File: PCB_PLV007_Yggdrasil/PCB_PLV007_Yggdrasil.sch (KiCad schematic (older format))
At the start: 16 parts

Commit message: Work on Heimdal and Yggdrasil
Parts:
- added C9, C? (x3): 0.1uF, symbol Device:C
- added C?: 1uF, symbol Device:C
- added D4, D?: LED, symbol Device:LED
- added JP?: Jumper_3_Open, symbol Jumper:Jumper_3_Open
- added Q4: Q_NMOS_GDS, symbol Device:Q_NMOS_GDS
- added Q5: Q_PMOS_GDS, symbol Device:Q_PMOS_GDS
- added R13, R18: 47K, symbol Device:R_US
- added R20, R? (x3): 1K, symbol Device:R_US
- added R22, R24, R28: 100K, symbol Device:R_US
- added R27: 700K, symbol Device:R_US
- added R? (x2): 10K, symbol Device:R_US
- added U7: BME280, Package_LGA:Bosch_LGA-8_2.5x2.5mm_P0.65mm_ClockwisePinNumbering, symbol Sensor:BME280
- added U?: 74HC21, Package_SO:SOIC-14_3.9x8.7mm_P1.27mm, symbol boringlib:74HC21
- added U? (x3): LM2902, symbol Amplifier_Operational:LM2902
- F1: renamed from F?; value Fuse -> 2A
- F2: renamed from F?; value Fuse -> 15A
- R21: renamed from R?; value R_US -> 1K
- R26: renamed from R?; value R_US -> 120
- gave numbers to parts that had none: 12
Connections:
- net labels added: +28V, C_SENSE, I2C_SCL, I2C_SDA, LOAD_SWITCH_ON, MCU_QB_INPUT, MCU_UHB_INPUT, UHB_MASTER, V_SENSE
- net labels removed: +24V, CURRENT_SENSE, LOAD_SWITCH_nON
- wire segments 75 -> 166
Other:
- moved on the sheet: C8, D1, F1, F2, J1, J2, JP1, NCLO1, Q3, R19, R21, R23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

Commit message: First version of Yggdrasil schematics complete
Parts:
- removed C9, C? (x2): 0.1uF, symbol Device:C
- removed D4, D?: LED, symbol Device:LED
- removed F2: 15A, symbol Device:Fuse
- removed J2: UMBILICAL_MASTER, symbol Connector_Generic:Conn_01x02
- removed Q3: Q_NPN_BCE, symbol Device:Q_NPN_BCE
- removed Q4: Q_NMOS_GDS, symbol Device:Q_NMOS_GDS
- removed Q5: Q_PMOS_GDS, symbol Device:Q_PMOS_GDS
- removed R20, R21, R? (x3): 1K, symbol Device:R_US
- removed R22, R24, R28: 100K, symbol Device:R_US
- removed R23: 2.7K, symbol Device:R_US
- removed R25, R? (x2): 10K, symbol Device:R_US
- removed R27: 700K, symbol Device:R_US
- removed U9: BTS50055-1TMA, Package_TO_SOT_SMD:TO-263-7_TabPin4, symbol Power_Management:BTS50055-1TMA
- removed U?: 74HC21, Package_SO:SOIC-14_3.9x8.7mm_P1.27mm, symbol boringlib:74HC21
- removed U? (x3): LM2902, symbol Amplifier_Operational:LM2902
- added C?: 0.1uF, symbol Device:C
- added C?: 10uF, symbol Device:C
- added C?: 1uF, symbol Device:C
- added R? (x3): 0, symbol Device:R_US
- added VR?: R-78C12-1.0, BoringFootprints:Recom_R-78c-1.0, symbol boringlib:R-78C12-1.0
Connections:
- net UMBILICAL_HEARTBEAT is gone; now on net UHB: R19.2
- net +12V: now also C?.1, C?.1, VR?.3 (+VOUT)
- net +28V: now also C?.1, VR?.1 (+VIN)
- net +5V: now also R?.2, R?.2, R?.2
- net AvionicsHeartbeatTemplate/HEARTBEAT_INPUT_5: now also R?.1
- net AvionicsHeartbeatTemplate/HEARTBEAT_INPUT_6: now also R?.1
- net AvionicsHeartbeatTemplate/HEARTBEAT_INPUT_7: now also R?.1
- net GND: now also C?.2, C?.2, C?.2, VR?.2 (GND)
- net HEARTBEAT_RESTART: now also NCLO1.32 (PA4/ADC/SPI1_SSEL/DAC)
- net V_SENSE: now also NCLO1.53 (PA7/ADC/SPI1_MOSI/PWM3_2); no longer NCLO1.32 (PA4/ADC/SPI1_SSEL/DAC)
- net UHB: now reaches NCLO1.75 (PA3/UART2_RX)
- net LOAD_SWITCH_ON renamed LOAD_SWITCH
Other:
- note added: "UHB and\nLoad Switch"
- moved on the sheet: C8, C?, JP1, JP?, NCLO1, R13, R18, R26, U7, U8

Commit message: Odin initial schematics ready for review
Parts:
- added C?: 0.1uF, symbol Device:C
- added C?: 10uF, symbol Device:C
- added C? (x2): 1uF, symbol Device:C
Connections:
- net +12V: now also C?.1, C?.1, C?.1, C?.1
- net GND: now also C?.2, C?.2, C?.2, C?.2
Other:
- note added: "QuantumBeat Slave"
- note removed: "QuantumBeat"
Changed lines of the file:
@@
 F15 "HEARTBEAT_BUFF" O R 9500 1350 50
 $EndSheet
-Text Notes 7950 1800 0    118  ~ 0
-QuantumBeat
+Text Notes 7650 1800 0    118  ~ 0
+QuantumBeat Slave
 $Comp
 L boringlib:NUCLEO-L476RG NCLO1
@@
 Text Label 6800 1100 0    50   ~ 0
 C_SAFE
+$Comp
+L power:+12V #PWR?
+U 1 1 5FC9527D
+P 2600 2200
+F 0 "#PWR?" H 2600 2050 50  0001 C CNN
+F 1 "+12V" H 2615 2373 50  0000 C CNN
+F 2 "" H 2600 2200 50  0001 C CNN
+F 3 "" H 2600 2200 50  0001 C CNN
+	1    2600 2200
+	1    0    0    -1
+$EndComp
+Wire Wire Line
+	3400 2650 3000 2650
+Connection ~ 3400 2650
+Wire Wire Line
+	3000 2650 2600 2650
+Connection ~ 3000 2650
+Wire Wire Line
+	3800 2650 3800 2700
+Connection ~ 3800 2650
+Wire Wire Line
+	3800 2650 3400 2650
+Connection ~ 2600 2250
+Wire Wire Line
+	2600 2250 2600 2200
+Connection ~ 3400 2250
+Wire Wire Line
+	3800 2250 3800 2300
+Wire Wire Line
+	3400 2250 3800 2250
+Connection ~ 3000 2250
+Wire Wire Line
+	3400 2250 3400 2300
+Wire Wire Line
+	3000 2250 3400 2250
+Wire Wire Line
+	3000 2250 3000 2300
+Wire Wire Line
+	2600 2250 3000 2250
+Wire Wire Line
+	3400 2600 3400 2650
+$Comp
+L Device:C C?
+U 1 1 5FC4A6FE
+P 3400 2450
+F 0 "C?" H 3515 2496 50  0000 L CNN
+F 1 "1uF" H 3515 2405 50  0000 L CNN
+F 2 "" H 3438 2300 50  0001 C CNN
+F 3 "~" H 3400 2450 50  0001 C CNN
+	1    3400 2450
+	1    0    0    -1
+$EndComp
+Wire Wire Line
+	3000 2600 3000 2650
+$Comp
+L Device:C C?
+U 1 1 5FC44A37
+P 3000 2450
+F 0 "C?" H 3115 2496 50  0000 L CNN
+F 1 "1uF" H 3115 2405 50  0000 L CNN
+F 2 "" H 3038 2300 50  0001 C CNN
+F 3 "~" H 3000 2450 50  0001 C CNN
+	1    3000 2450
+	1    0    0    -1
+$EndComp
+Wire Wire Line
+	2600 2600 2600 2650
+Wire Wire Line
+	2600 2300 2600 2250
+$Comp
+L Device:C C?
+U 1 1 5FC3EF1E
+P 2600 2450
+F 0 "C?" H 2715 2496 50  0000 L CNN
+F 1 "10uF" H 2715 2405 50  0000 L CNN
+F 2 "" H 2638 2300 50  0001 C CNN
+F 3 "~" H 2600 2450 50  0001 C CNN
+	1    2600 2450
+	1    0    0    -1
+$EndComp
+$Comp
+L power:GND #PWR?
+U 1 1 5FC392F5
+P 3800 2700
+F 0 "#PWR?" H 3800 2450 50  0001 C CNN
+F 1 "GND" H 3805 2527 50  0000 C CNN
+F 2 "" H 3800 2700 50  0001 C CNN
+F 3 "" H 3800 2700 50  0001 C CNN
+	1    3800 2700
+	1    0    0    -1
+$EndComp
+Wire Wire Line
+	3800 2600 3800 2650
+$Comp
+L Device:C C?
+U 1 1 5FC392EA
+P 3800 2450
+F 0 "C?" H 3915 2496 50  0000 L CNN
+F 1 "0.1uF" H 3915 2405 50  0000 L CNN
+F 2 "" H 3838 2300 50  0001 C CNN
+F 3 "~" H 3800 2450 50  0001 C CNN
+	1    3800 2450
+	1    0    0    -1
+$EndComp
 $EndSCHEMATC

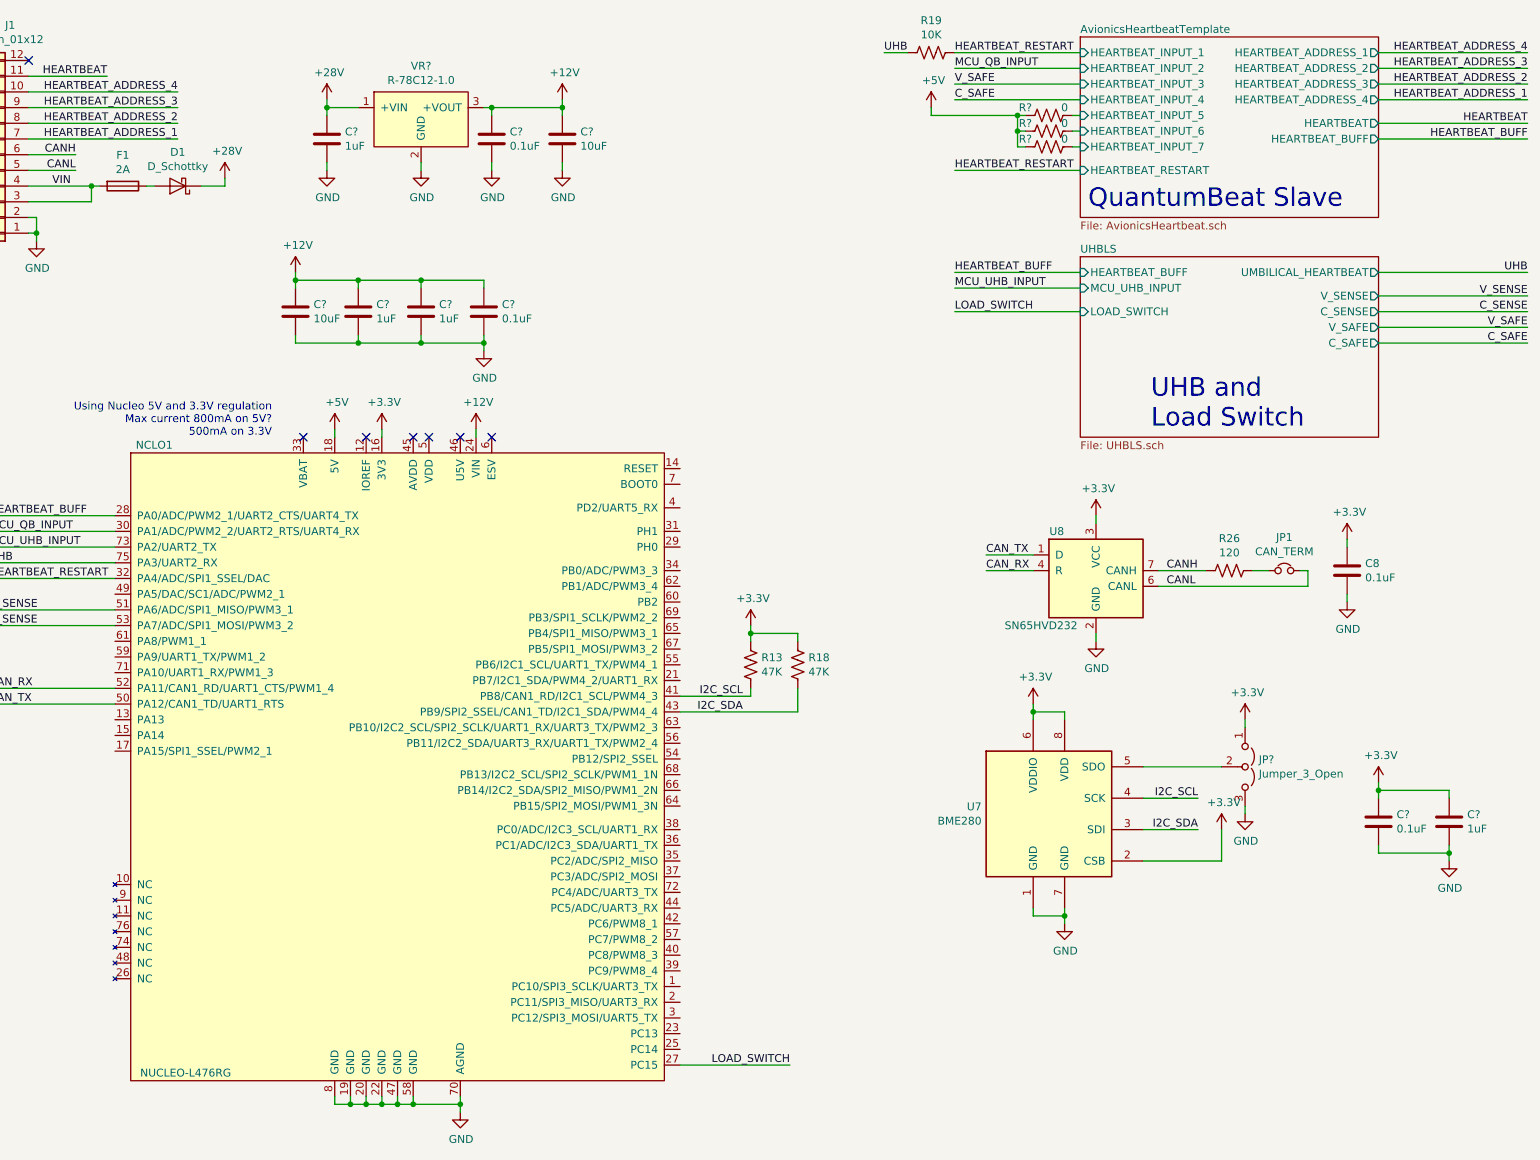
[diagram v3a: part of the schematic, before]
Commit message: Make Yggdrasil pass ERC
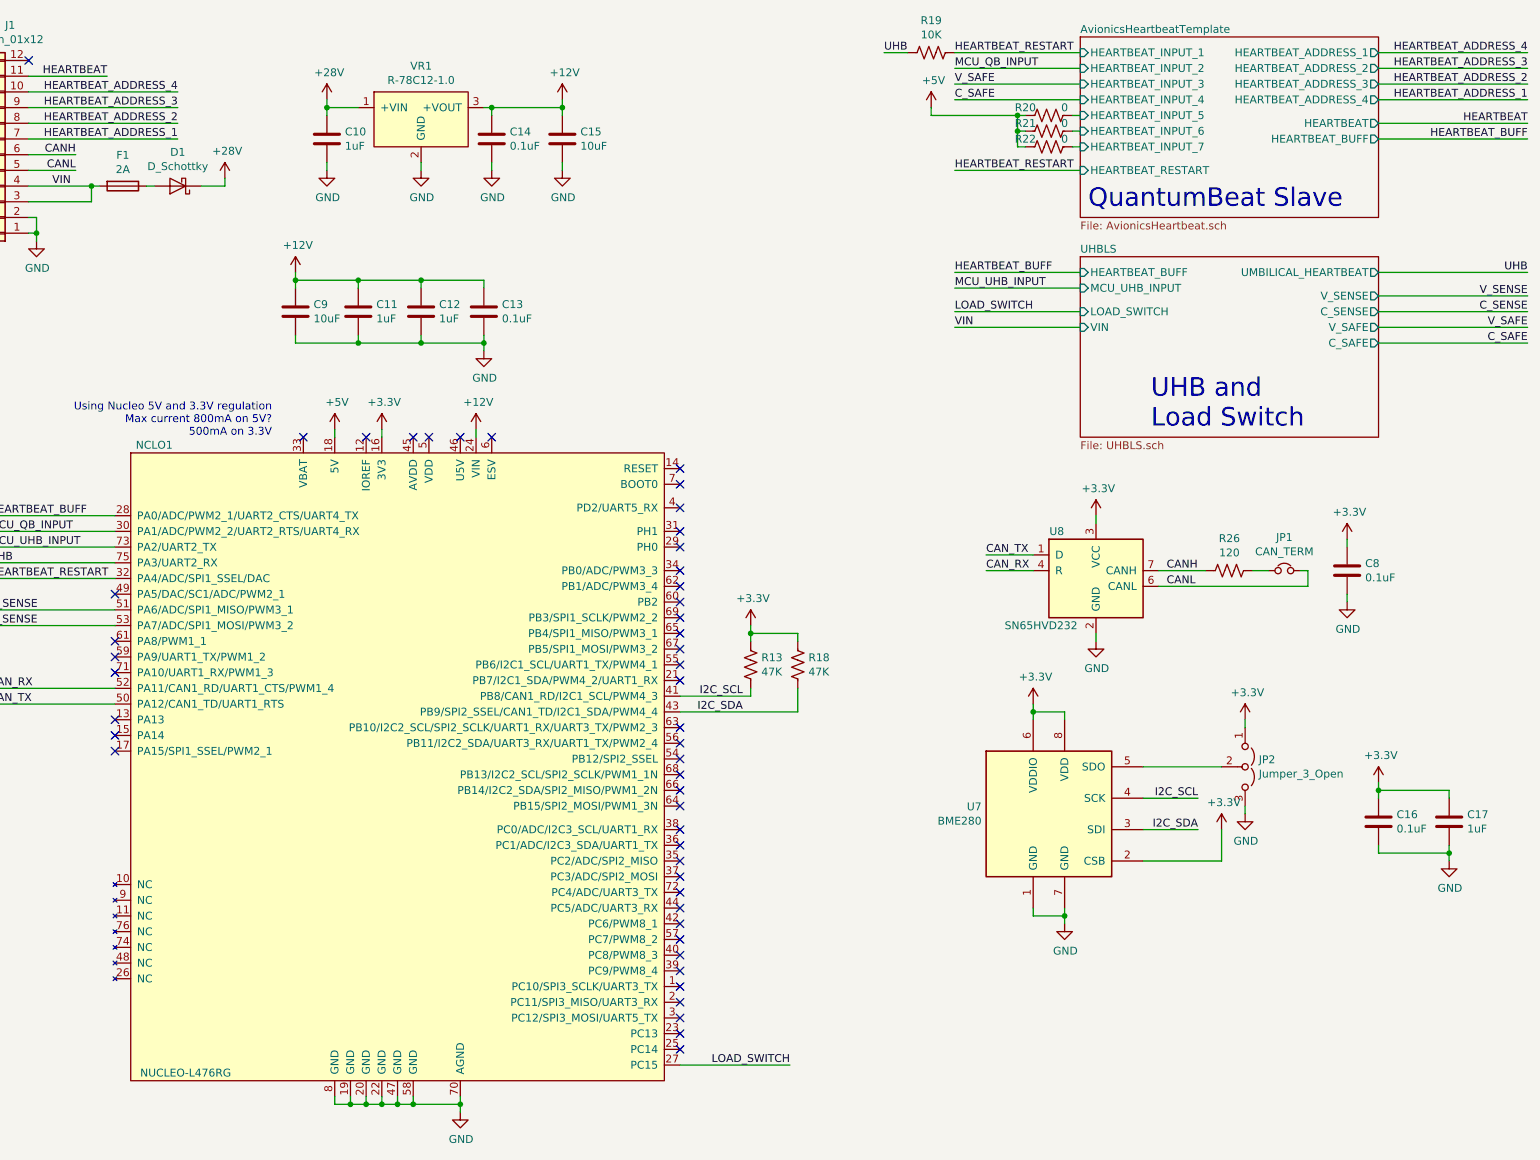
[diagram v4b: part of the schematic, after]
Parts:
- gave numbers to parts that had none: 14
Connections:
- no-connect marks 7 -> 48
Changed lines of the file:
@@
 I2C_SDA
 $Comp
-L power:+3.3V #PWR?
+L power:+3.3V #PWR0110
 U 1 1 5FCF0BBE
 P 8500 5750
-F 0 "#PWR?" H 8500 5600 50  0001 C CNN
+F 0 "#PWR0110" H 8500 5600 50  0001 C CNN
 F 1 "+3.3V" H 8515 5923 50  0000 C CNN
 F 2 "" H 8500 5750 50  0001 C CNN
@@
 	8500 5950 8500 5750
 $Comp
-L power:+3.3V #PWR?
+L power:+3.3V #PWR0111
 U 1 1 5FCF6D3B
 P 8650 5050
-F 0 "#PWR?" H 8650 4900 50  0001 C CNN
+F 0 "#PWR0111" H 8650 4900 50  0001 C CNN
 F 1 "+3.3V" H 8665 5223 50  0000 C CNN
 F 2 "" H 8650 5050 50  0001 C CNN
@@
 $EndComp
 $Comp
-L Jumper:Jumper_3_Open JP?
+L Jumper:Jumper_3_Open JP2
 U 1 1 5FCF7D7F
 P 8650 5350
-F 0 "JP?" V 8604 5437 50  0000 L CNN
+F 0 "JP2" V 8604 5437 50  0000 L CNN
 F 1 "Jumper_3_Open" V 8695 5437 50  0000 L CNN
 F 2 "" H 8650 5350 50  0001 C CNN
@@
 	8650 5600 8650 5650
 $Comp
-L power:GND #PWR?
+L power:GND #PWR0112
 U 1 1 5FD08740
 P 8650 5650
-F 0 "#PWR?" H 8650 5400 50  0001 C CNN
+F 0 "#PWR0112" H 8650 5400 50  0001 C CNN
 F 1 "GND" H 8655 5477 50  0000 C CNN
 F 2 "" H 8650 5650 50  0001 C CNN
@@
 $EndComp
 $Comp
-L power:+3.3V #PWR?
+L power:+3.3V #PWR0114
 U 1 1 5FD19B79
 P 9500 5450
-F 0 "#PWR?" H 9500 5300 50  0001 C CNN
+F 0 "#PWR0114" H 9500 5300 50  0001 C CNN
 F 1 "+3.3V" H 9515 5623 50  0000 C CNN
 F 2 "" H 9500 5450 50  0001 C CNN
@@
 $EndComp
 $Comp
-L Device:C C?
+L Device:C C16
 U 1 1 5FD19B8D
 P 9500 5700
-F 0 "C?" H 9615 5746 50  0000 L CNN
+F 0 "C16" H 9615 5746 50  0000 L CNN
 F 1 "0.1uF" H 9615 5655 50  0000 L CNN
 F 2 "" H 9538 5550 50  0001 C CNN
@@
 	9500 5550 9500 5500
 $Comp
-L power:GND #PWR?
+L power:GND #PWR0115
 U 1 1 5FD24EA9
 P 9950 5950
-F 0 "#PWR?" H 9950 5700 50  0001 C CNN
+F 0 "#PWR0115" H 9950 5700 50  0001 C CNN
 F 1 "GND" H 9955 5777 50  0000 C CNN
 F 2 "" H 9950 5950 50  0001 C CNN
@@
 $EndComp
 $Comp
-L Device:C C?
+L Device:C C17
 U 1 1 5FD24EB3
 P 9950 5700
-F 0 "C?" H 10065 5746 50  0000 L CNN
+F 0 "C17" H 10065 5746 50  0000 L CNN
 F 1 "1uF" H 10065 5655 50  0000 L CNN
 F 2 "" H 9988 5550 50  0001 C CNN
@@
 F8 "C_SAFE" O R 9500 2650 50
 F9 "V_SAFE" O R 9500 2550 50
+F10 "VIN" I L 7600 2550 50
 $EndSheet
 Text Notes 8050 3200 0    118  ~ 0
@@
 	9950 5900 9950 5950
 $Comp
-L boringlib:R-78C12-1.0 VR?
+L boringlib:R-78C12-1.0 VR1
 U 1 1 5FD31019
 P 3400 1150
-F 0 "VR?" H 3400 1415 50  0000 C CNN
+F 0 "VR1" H 3400 1415 50  0000 C CNN
 F 1 "R-78C12-1.0" H 3400 1324 50  0000 C CNN
 F 2 "BoringFootprints:Recom_R-78c-1.0" H 3600 850 50  0001 C CNN
@@
 $EndComp
 $Comp
-L power:+28V #PWR?
+L power:+28V #PWR0116
 U 1 1 5FD31983
 P 2800 1100
-F 0 "#PWR?" H 2800 950 50  0001 C CNN
+F 0 "#PWR0116" H 2800 950 50  0001 C CNN
 F 1 "+28V" H 2815 1273 50  0000 C CNN
 F 2 "" H 3050 1150 50  0001 C CNN
@@
 	4300 1150 4300 1100
 $Comp
-L power:+12V #PWR?
+L power:+12V #PWR0117
 U 1 1 5FD3C5DB
 P 4300 1100
-F 0 "#PWR?" H 4300 950 50  0001 C CNN
+F 0 "#PWR0117" H 4300 950 50  0001 C CNN
 F 1 "+12V" H 4315 1273 50  0000 C CNN
 F 2 "" H 4300 1100 50  0001 C CNN
@@
 $EndComp
 $Comp
-L power:GND #PWR?
+L power:GND #PWR0119
 U 1 1 5FD4114D
 P 3400 1550
-F 0 "#PWR?" H 3400 1300 50  0001 C CNN
+F 0 "#PWR0119" H 3400 1300 50  0001 C CNN
 F 1 "GND" H 3405 1377 50  0000 C CNN
 F 2 "" H 3400 1550 50  0001 C CNN
@@
 $EndComp
 $Comp
-L Device:C C?
+L Device:C C14
 U 1 1 5FD426E2
 P 3850 1350
-F 0 "C?" H 3965 1396 50  0000 L CNN
+F 0 "C14" H 3965 1396 50  0000 L CNN
 F 1 "0.1uF" H 3965 1305 50  0000 L CNN
 F 2 "" H 3888 1200 50  0001 C CNN
@@
 	3850 1150 4300 1150
 $Comp
-L Device:C C?
+L Device:C C15
 U 1 1 5FD4A5ED
 P 4300 1350
-F 0 "C?" H 4415 1396 50  0000 L CNN
+F 0 "C15" H 4415 1396 50  0000 L CNN
 F 1 "10uF" H 4415 1305 50  0000 L CNN
 F 2 "" H 4338 1200 50  0001 C CNN
@@
 	4300 1500 4300 1550
 $Comp
-L power:GND #PWR?
+L power:GND #PWR0120
 U 1 1 5FD5522F
 P 3850 1550
-F 0 "#PWR?" H 3850 1300 50  0001 C CNN
+F 0 "#PWR0120" H 3850 1300 50  0001 C CNN
 F 1 "GND" H 3855 1377 50  0000 C CNN
 F 2 "" H 3850 1550 50  0001 C CNN
@@
 $EndComp
 $Comp
-L power:GND #PWR?
+L power:GND #PWR0123
 U 1 1 5FD55647
 P 4300 1550
-F 0 "#PWR?" H 4300 1300 50  0001 C CNN
+F 0 "#PWR0123" H 4300 1300 50  0001 C CNN
 F 1 "GND" H 4305 1377 50  0000 C CNN
 F 2 "" H 4300 1550 50  0001 C CNN
@@
 $EndComp
 $Comp
-L Device:C C?
+L Device:C C10
 U 1 1 5FD55D12
 P 2800 1350
-F 0 "C?" H 2915 1396 50  0000 L CNN
+F 0 "C10" H 2915 1396 50  0000 L CNN
 F 1 "1uF" H 2915 1305 50  0000 L CNN
 F 2 "" H 2838 1200 50  0001 C CNN
@@
 	2800 1500 2800 1550
 $Comp
-L power:GND #PWR?
+L power:GND #PWR0124
 U 1 1 5FD5E222
 P 2800 1550
-F 0 "#PWR?" H 2800 1300 50  0001 C CNN
+F 0 "#PWR0124" H 2800 1300 50  0001 C CNN
 F 1 "GND" H 2805 1377 50  0000 C CNN
 F 2 "" H 2800 1550 50  0001 C CNN
@@
 	7600 1300 7550 1300
 $Comp
-L Device:R_US R?
+L Device:R_US R20
 U 1 1 5FD93979
 P 7400 1200
-F 0 "R?" V 7350 1050 50  0000 C CNN
+F 0 "R20" V 7350 1050 50  0000 C CNN
 F 1 "0" V 7350 1300 50  0000 C CNN
 F 2 "" V 7440 1190 50  0001 C CNN
@@
 $EndComp
 $Comp
-L Device:R_US R?
+L Device:R_US R21
 U 1 1 5FD94AC1
 P 7400 1300
-F 0 "R?" V 7350 1150 50  0000 C CNN
+F 0 "R21" V 7350 1150 50  0000 C CNN
 F 1 "0" V 7350 1400 50  0000 C CNN
 F 2 "" V 7440 1290 50  0001 C CNN
@@
 $EndComp
 $Comp
-L Device:R_US R?
+L Device:R_US R22
 U 1 1 5FD94E5D
 P 7400 1400
-F 0 "R?" V 7350 1250 50  0000 C CNN
+F 0 "R22" V 7350 1250 50  0000 C CNN
 F 1 "0" V 7350 1500 50  0000 C CNN
 F 2 "" V 7440 1390 50  0001 C CNN
@@
 	6650 1200 7200 1200
 $Comp
-L power:+5V #PWR?
+L power:+5V #PWR0125
 U 1 1 5FDA7193
 P 6650 1150
-F 0 "#PWR?" H 6650 1000 50  0001 C CNN
+F 0 "#PWR0125" H 6650 1000 50  0001 C CNN
 F 1 "+5V" H 6665 1323 50  0000 C CNN
 F 2 "" H 6650 1150 50  0001 C CNN
@@
 C_SAFE
 $Comp
-L power:+12V #PWR?
+L power:+12V #PWR0126
 U 1 1 5FC9527D
 P 2600 2200
-F 0 "#PWR?" H 2600 2050 50  0001 C CNN
+F 0 "#PWR0126" H 2600 2050 50  0001 C CNN
 F 1 "+12V" H 2615 2373 50  0000 C CNN
 F 2 "" H 2600 2200 50  0001 C CNN
@@
 	3400 2600 3400 2650
 $Comp
-L Device:C C?
+L Device:C C12
 U 1 1 5FC4A6FE
 P 3400 2450
-F 0 "C?" H 3515 2496 50  0000 L CNN
+F 0 "C12" H 3515 2496 50  0000 L CNN
 F 1 "1uF" H 3515 2405 50  0000 L CNN
 F 2 "" H 3438 2300 50  0001 C CNN
@@
 	3000 2600 3000 2650
 $Comp
-L Device:C C?
+L Device:C C11
 U 1 1 5FC44A37
 P 3000 2450
-F 0 "C?" H 3115 2496 50  0000 L CNN
+F 0 "C11" H 3115 2496 50  0000 L CNN
 F 1 "1uF" H 3115 2405 50  0000 L CNN
 F 2 "" H 3038 2300 50  0001 C CNN
@@
 	2600 2300 2600 2250
 $Comp
-L Device:C C?
+L Device:C C9
 U 1 1 5FC3EF1E
 P 2600 2450
-F 0 "C?" H 2715 2496 50  0000 L CNN
+F 0 "C9" H 2715 2496 50  0000 L CNN
 F 1 "10uF" H 2715 2405 50  0000 L CNN
 F 2 "" H 2638 2300 50  0001 C CNN
@@
 $EndComp
 $Comp
-L power:GND #PWR?
+L power:GND #PWR0127
 U 1 1 5FC392F5
 P 3800 2700
-F 0 "#PWR?" H 3800 2450 50  0001 C CNN
+F 0 "#PWR0127" H 3800 2450 50  0001 C CNN
 F 1 "GND" H 3805 2527 50  0000 C CNN
 F 2 "" H 3800 2700 50  0001 C CNN
@@
 	3800 2600 3800 2650
 $Comp
-L Device:C C?
+L Device:C C13
 U 1 1 5FC392EA
 P 3800 2450
-F 0 "C?" H 3915 2496 50  0000 L CNN
+F 0 "C13" H 3915 2496 50  0000 L CNN
 F 1 "0.1uF" H 3915 2405 50  0000 L CNN
 F 2 "" H 3838 2300 50  0001 C CNN
@@
 	1    0    0    -1
 $EndComp
+NoConn ~ 5050 3450
+NoConn ~ 5050 3550
+NoConn ~ 5050 3700
+NoConn ~ 5050 3850
+NoConn ~ 5050 3950
+NoConn ~ 5050 4100
+NoConn ~ 5050 4200
+NoConn ~ 5050 4300
+NoConn ~ 5050 4400
+NoConn ~ 5050 4500
+NoConn ~ 5050 4600
+NoConn ~ 5050 4700
+NoConn ~ 5050 4800
+NoConn ~ 5050 5100
+NoConn ~ 5050 5200
+NoConn ~ 5050 5300
+NoConn ~ 5050 5400
+NoConn ~ 5050 5500
+NoConn ~ 5050 5600
+NoConn ~ 5050 5750
+NoConn ~ 5050 5850
+NoConn ~ 5050 5950
+NoConn ~ 5050 6050
+NoConn ~ 5050 6150
+NoConn ~ 5050 6250
+NoConn ~ 5050 6350
+NoConn ~ 5050 6450
+NoConn ~ 5050 6550
+NoConn ~ 5050 6650
+NoConn ~ 5050 6750
+NoConn ~ 5050 6850
+NoConn ~ 5050 6950
+NoConn ~ 5050 7050
+NoConn ~ 5050 7150
+NoConn ~ 1450 4250
+NoConn ~ 1450 4550
+NoConn ~ 1450 4650
+NoConn ~ 1450 4750
+NoConn ~ 1450 5050
+NoConn ~ 1450 5150
+NoConn ~ 1450 5250
+Text Label 6800 2550 0    50   ~ 0
+VIN
+Wire Wire Line
+	6800 2550 7600 2550
 $EndSCHEMATC
